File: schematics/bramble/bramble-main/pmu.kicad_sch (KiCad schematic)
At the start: 18 parts, among them J1 Conn_01x05_Pin, J6 Conn_01x03_Pin, SW1 STM_RESET, U3 STM32L031F6P6TR, U5 MCP1700x-120xxMB, Y1 Crystal

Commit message: pre-fab check-in of v2
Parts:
- renumbered C3 to C1, C4 to C2, C5 to C3, C24 to C4, C23 to C5, C21 to C7, C22 to C8, J6 to J2, R22 to R13, R23 to R14, R11 to R15, U5 to U4
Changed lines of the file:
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@@
 		(on_board yes)
 		(dnp no)
-		(property "Reference" "C23"
+		(property "Reference" "C5"
 			(at 161.29 123.1901 0)
 			(effects
@@
 			(project "bramble"
 				(path "/e35d7dcf-51bd-456f-89cf-e52d660079b4/df1d8afa-9717-44ff-901e-40cae4aada91"
-					(reference "C23")
+					(reference "C5")
 					(unit 1)
 				)
@@
 		(on_board yes)
 		(dnp no)
-		(property "Reference" "#U$07"
+		(property "Reference" "#U$012"
 			(at 92.71 90.17 0)
 			(effects
@@
 			(project "bramble"
 				(path "/e35d7dcf-51bd-456f-89cf-e52d660079b4/df1d8afa-9717-44ff-901e-40cae4aada91"
-					(reference "#U$07")
+					(reference "#U$012")
 					(unit 1)
 				)
@@
 		(on_board yes)
 		(dnp no)
-		(property "Reference" "#U$039"
+		(property "Reference" "#U$017"
 			(at 222.25 68.58 0)
 			(effects
@@
 			(project "bramble"
 				(path "/e35d7dcf-51bd-456f-89cf-e52d660079b4/df1d8afa-9717-44ff-901e-40cae4aada91"
-					(reference "#U$039")
+					(reference "#U$017")
 					(unit 1)
 				)
@@
 		(dnp no)
 		(fields_autoplaced yes)
-		(property "Reference" "C4"
+		(property "Reference" "C2"
 			(at 62.23 161.2899 0)
 			(effects
@@
 			(project "bramble"
 				(path "/e35d7dcf-51bd-456f-89cf-e52d660079b4/df1d8afa-9717-44ff-901e-40cae4aada91"
-					(reference "C4")
+					(reference "C2")
 					(unit 1)
 				)
@@
 		(dnp no)
 		(fields_autoplaced yes)
-		(property "Reference" "#PWR018"
+		(property "Reference" "#PWR011"
 			(at 125.095 158.115 0)
 			(effects
@@
 			(project ""
 				(path "/e35d7dcf-51bd-456f-89cf-e52d660079b4/df1d8afa-9717-44ff-901e-40cae4aada91"
-					(reference "#PWR018")
+					(reference "#PWR011")
 					(unit 1)
 				)
@@
 		(dnp no)
 		(fields_autoplaced yes)
-		(property "Reference" "#PWR05"
+		(property "Reference" "#PWR010"
 			(at 123.19 172.72 0)
 			(effects
@@
 			(project ""
 				(path "/e35d7dcf-51bd-456f-89cf-e52d660079b4/df1d8afa-9717-44ff-901e-40cae4aada91"
-					(reference "#PWR05")
+					(reference "#PWR010")
 					(unit 1)
 				)
@@
 		(dnp no)
 		(fields_autoplaced yes)
-		(property "Reference" "C5"
+		(property "Reference" "C3"
 			(at 76.2 161.2899 0)
 			(effects
@@
 			(project "bramble"
 				(path "/e35d7dcf-51bd-456f-89cf-e52d660079b4/df1d8afa-9717-44ff-901e-40cae4aada91"
-					(reference "C5")
+					(reference "C3")
 					(unit 1)
 				)
@@
 		(on_board yes)
 		(dnp no)
-		(property "Reference" "C22"
+		(property "Reference" "C8"
 			(at 226.06 62.2299 0)
 			(effects
@@
 			(project "bramble"
 				(path "/e35d7dcf-51bd-456f-89cf-e52d660079b4/df1d8afa-9717-44ff-901e-40cae4aada91"
-					(reference "C22")
+					(reference "C8")
 					(unit 1)
 				)
@@
 		(dnp no)
 		(fields_autoplaced yes)
-		(property "Reference" "#PWR016"
+		(property "Reference" "#PWR09"
 			(at 58.42 154.94 0)
 			(effects
@@
 			(project "bramble"
 				(path "/e35d7dcf-51bd-456f-89cf-e52d660079b4/df1d8afa-9717-44ff-901e-40cae4aada91"
-					(reference "#PWR016")
+					(reference "#PWR09")
 					(unit 1)
 				)
@@
 		(on_board yes)
 		(dnp no)
-		(property "Reference" "R22"
+		(property "Reference" "R13"
 			(at 79.502 84.328 90)
 			(effects
@@
 			(project "bramble"
 				(path "/e35d7dcf-51bd-456f-89cf-e52d660079b4/df1d8afa-9717-44ff-901e-40cae4aada91"
-					(reference "R22")
+					(reference "R13")
 					(unit 1)
 				)
@@
 		(on_board yes)
 		(dnp no)
-		(property "Reference" "C21"
+		(property "Reference" "C7"
 			(at 213.995 50.1649 0)
 			(effects
@@
 			(project "bramble"
 				(path "/e35d7dcf-51bd-456f-89cf-e52d660079b4/df1d8afa-9717-44ff-901e-40cae4aada91"
-					(reference "C21")
+					(reference "C7")
 					(unit 1)
 				)
@@
 		(on_board yes)
 		(dnp no)
-		(property "Reference" "C24"
+		(property "Reference" "C4"
 			(at 132.08 123.1901 0)
 			(effects
@@
 			(project "bramble"
 				(path "/e35d7dcf-51bd-456f-89cf-e52d660079b4/df1d8afa-9717-44ff-901e-40cae4aada91"
-					(reference "C24")
+					(reference "C4")
 					(unit 1)
 				)
@@
 		(dnp no)
 		(fields_autoplaced yes)
-		(property "Reference" "U5"
+		(property "Reference" "U4"
 			(at 148.59 111.76 0)
 			(effects
@@
 			(project ""
 				(path "/e35d7dcf-51bd-456f-89cf-e52d660079b4/df1d8afa-9717-44ff-901e-40cae4aada91"
-					(reference "U5")
+					(reference "U4")
 					(unit 1)
 				)
@@
 		(dnp no)
 		(fields_autoplaced yes)
-		(property "Reference" "R11"
+		(property "Reference" "R15"
 			(at 165.1 44.45 90)
 			(effects
@@
 			(project ""
 				(path "/e35d7dcf-51bd-456f-89cf-e52d660079b4/df1d8afa-9717-44ff-901e-40cae4aada91"
-					(reference "R11")
+					(reference "R15")
 					(unit 1)
 				)
@@
 		(on_board yes)
 		(dnp no)
-		(property "Reference" "#U$034"
+		(property "Reference" "#U$016"
 			(at 210.185 67.31 0)
 			(effects
@@
 			(project "bramble"
 				(path "/e35d7dcf-51bd-456f-89cf-e52d660079b4/df1d8afa-9717-44ff-901e-40cae4aada91"
-					(reference "#U$034")
+					(reference "#U$016")
 					(unit 1)
 				)
@@
 		(dnp no)
 		(fields_autoplaced yes)
-		(property "Reference" "#PWR014"
+		(property "Reference" "#PWR08"
 			(at 52.07 40.64 0)
 			(effects
@@
 			(project "bramble"
 				(path "/e35d7dcf-51bd-456f-89cf-e52d660079b4/df1d8afa-9717-44ff-901e-40cae4aada91"
-					(reference "#PWR014")
+					(reference "#PWR08")
 					(unit 1)
 				)
@@
 		(on_board yes)
 		(dnp no)
-		(property "Reference" "#U$09"
+		(property "Reference" "#U$014"
 			(at 196.85 85.09 0)
 			(effects
@@
 			(project "bramble"
 				(path "/e35d7dcf-51bd-456f-89cf-e52d660079b4/df1d8afa-9717-44ff-901e-40cae4aada91"
-					(reference "#U$09")
+					(reference "#U$014")
 					(unit 1)
 				)
@@
 		(on_board yes)
 		(dnp no)
-		(property "Reference" "#U$04"
+		(property "Reference" "#U$09"
 			(at 52.07 80.01 0)
 			(effects
@@
 			(project "bramble"
 				(path "/e35d7dcf-51bd-456f-89cf-e52d660079b4/df1d8afa-9717-44ff-901e-40cae4aada91"
-					(reference "#U$04")
+					(reference "#U$09")
 					(unit 1)
 				)
@@
 		(on_board yes)
 		(dnp no)
-		(property "Reference" "#U$010"
+		(property "Reference" "#U$013"
 			(at 148.59 135.89 0)
 			(effects
@@
 			(project "bramble"
 				(path "/e35d7dcf-51bd-456f-89cf-e52d660079b4/df1d8afa-9717-44ff-901e-40cae4aada91"
-					(reference "#U$010")
+					(reference "#U$013")
 					(unit 1)
 				)
@@
 		(on_board yes)
 		(dnp no)
-		(property "Reference" "#U$05"
+		(property "Reference" "#U$010"
 			(at 58.42 179.07 0)
 			(effects
@@
 			(project "bramble"
 				(path "/e35d7dcf-51bd-456f-89cf-e52d660079b4/df1d8afa-9717-44ff-901e-40cae4aada91"
-					(reference "#U$05")
+					(reference "#U$010")
 					(unit 1)
 				)
@@
 		(on_board yes)
 		(dnp no)
-		(property "Reference" "R23"
+		(property "Reference" "R14"
 			(at 84.582 84.328 90)
 			(effects
@@
 			(project "bramble"
 				(path "/e35d7dcf-51bd-456f-89cf-e52d660079b4/df1d8afa-9717-44ff-901e-40cae4aada91"
-					(reference "R23")
+					(reference "R14")
 					(unit 1)
 				)
@@
 		(dnp no)
 		(fields_autoplaced yes)
-		(property "Reference" "#PWR017"
+		(property "Reference" "#PWR012"
 			(at 165.1 116.84 0)
 			(effects
@@
 			(project "bramble"
 				(path "/e35d7dcf-51bd-456f-89cf-e52d660079b4/df1d8afa-9717-44ff-901e-40cae4aada91"
-					(reference "#PWR017")
+					(reference "#PWR012")
 					(unit 1)
 				)
@@
 		(on_board yes)
 		(dnp no)
-		(property "Reference" "#U$08"
+		(property "Reference" "#U$015"
 			(at 203.2 64.77 0)
 			(effects
@@
 			(project "bramble"
 				(path "/e35d7dcf-51bd-456f-89cf-e52d660079b4/df1d8afa-9717-44ff-901e-40cae4aada91"
-					(reference "#U$08")
+					(reference "#U$015")
 					(unit 1)
 				)
@@
 		(dnp no)
 		(fields_autoplaced yes)
-		(property "Reference" "#PWR015"
+		(property "Reference" "#PWR013"
 			(at 165.735 71.12 0)
 			(effects
@@
 			(project "bramble"
 				(path "/e35d7dcf-51bd-456f-89cf-e52d660079b4/df1d8afa-9717-44ff-901e-40cae4aada91"
-					(reference "#PWR015")
+					(reference "#PWR013")
 					(unit 1)
 				)
@@
 		(dnp no)
 		(fields_autoplaced yes)
-		(property "Reference" "C3"
+		(property "Reference" "C1"
 			(at 49.53 161.2899 0)
 			(effects
@@
 			(project ""
 				(path "/e35d7dcf-51bd-456f-89cf-e52d660079b4/df1d8afa-9717-44ff-901e-40cae4aada91"
-					(reference "C3")
+					(reference "C1")
 					(unit 1)
 				)
@@
 		(on_board yes)
 		(dnp no)
-		(property "Reference" "#U$06"
+		(property "Reference" "#U$011"
 			(at 80.01 110.49 0)
 			(effects
@@
 			(project "bramble"
 				(path "/e35d7dcf-51bd-456f-89cf-e52d660079b4/df1d8afa-9717-44ff-901e-40cae4aada91"
-					(reference "#U$06")
+					(reference "#U$011")
 					(unit 1)
 				)
@@
 		(dnp no)
 		(fields_autoplaced yes)
-		(property "Reference" "J6"
+		(property "Reference" "J2"
 			(at 111.125 153.67 0)
 			(effects
@@
 			(project ""
 				(path "/e35d7dcf-51bd-456f-89cf-e52d660079b4/df1d8afa-9717-44ff-901e-40cae4aada91"
-					(reference "J6")
-					(unit 1)
-				)
+					(reference "J2")
+					(unit 1)
+				)

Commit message: Checking before rollback
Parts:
- renumbered J2 to PWR1, J1 to STM_DEBUG1, D1 to STM_STATUS1, U3 to U2, U4 to U3
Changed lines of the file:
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@@
 		(dnp no)
 		(fields_autoplaced yes)
-		(property "Reference" "J1"
+		(property "Reference" "STM_DEBUG1"
 			(at 34.925 40.64 0)
 			(effects
@@
 			(project ""
 				(path "/e35d7dcf-51bd-456f-89cf-e52d660079b4/df1d8afa-9717-44ff-901e-40cae4aada91"
-					(reference "J1")
+					(reference "STM_DEBUG1")
 					(unit 1)
 				)
@@
 		(dnp no)
 		(fields_autoplaced yes)
-		(property "Reference" "D1"
+		(property "Reference" "STM_STATUS1"
 			(at 86.36 93.9164 90)
 			(effects
@@
 			(project ""
 				(path "/e35d7dcf-51bd-456f-89cf-e52d660079b4/df1d8afa-9717-44ff-901e-40cae4aada91"
-					(reference "D1")
+					(reference "STM_STATUS1")
 					(unit 1)
 				)
@@
 		(dnp no)
 		(fields_autoplaced yes)
-		(property "Reference" "U4"
+		(property "Reference" "U3"
 			(at 148.59 111.76 0)
 			(effects
@@
 			(project ""
 				(path "/e35d7dcf-51bd-456f-89cf-e52d660079b4/df1d8afa-9717-44ff-901e-40cae4aada91"
-					(reference "U4")
+					(reference "U3")
 					(unit 1)
 				)
@@
 		(dnp no)
 		(fields_autoplaced yes)
-		(property "Reference" "U3"
+		(property "Reference" "U2"
 			(at 124.46 38.1 0)
 			(effects
@@
 			(project "bramble"
 				(path "/e35d7dcf-51bd-456f-89cf-e52d660079b4/df1d8afa-9717-44ff-901e-40cae4aada91"
-					(reference "U3")
+					(reference "U2")
 					(unit 1)
 				)
@@
 		(dnp no)
 		(fields_autoplaced yes)
-		(property "Reference" "J2"
+		(property "Reference" "PWR1"
 			(at 111.125 153.67 0)
 			(effects
@@
 			(project ""
 				(path "/e35d7dcf-51bd-456f-89cf-e52d660079b4/df1d8afa-9717-44ff-901e-40cae4aada91"
-					(reference "J2")
-					(unit 1)
-				)
+					(reference "PWR1")
+					(unit 1)
+				)

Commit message: Check in some of the v3 change
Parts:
- renumbered STM_STATUS1 to D1, STM_DEBUG1 to J1, PWR1 to J2
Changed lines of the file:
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@@
 		(dnp no)
 		(fields_autoplaced yes)
-		(property "Reference" "STM_DEBUG1"
+		(property "Reference" "J1"
 			(at 34.925 40.64 0)
 			(effects
@@
 			(project ""
 				(path "/e35d7dcf-51bd-456f-89cf-e52d660079b4/df1d8afa-9717-44ff-901e-40cae4aada91"
-					(reference "STM_DEBUG1")
+					(reference "J1")
 					(unit 1)
 				)
@@
 		(dnp no)
 		(fields_autoplaced yes)
-		(property "Reference" "STM_STATUS1"
+		(property "Reference" "D1"
 			(at 86.36 93.9164 90)
 			(effects
@@
 			(project ""
 				(path "/e35d7dcf-51bd-456f-89cf-e52d660079b4/df1d8afa-9717-44ff-901e-40cae4aada91"
-					(reference "STM_STATUS1")
+					(reference "D1")
 					(unit 1)
 				)
@@
 		(dnp no)
 		(fields_autoplaced yes)
-		(property "Reference" "PWR1"
+		(property "Reference" "J2"
 			(at 111.125 153.67 0)
 			(effects
@@
 			(project ""
 				(path "/e35d7dcf-51bd-456f-89cf-e52d660079b4/df1d8afa-9717-44ff-901e-40cae4aada91"
-					(reference "PWR1")
-					(unit 1)
-				)
+					(reference "J2")
+					(unit 1)
+				)

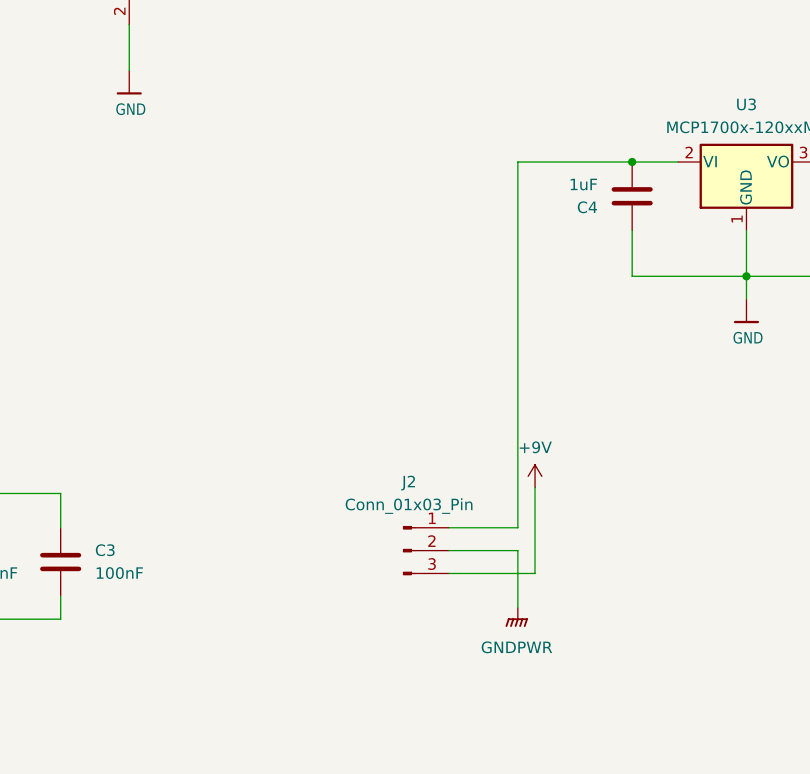
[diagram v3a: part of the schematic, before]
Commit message: Switch to 2x 2 pin JST connectors and wire them in series on board
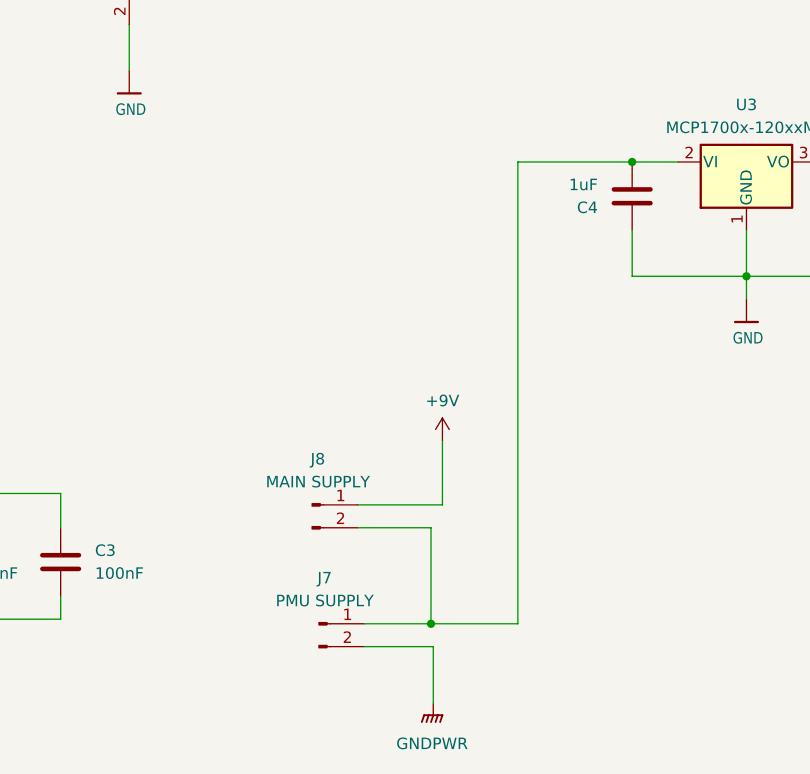
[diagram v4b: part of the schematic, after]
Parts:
- removed J2: Conn_01x03_Pin, Connector_JST:JST_XH_B3B-XH-AM_1x03_P2.50mm_Vertical, symbol Connector:Conn_01x03_Pin
- added J7: PMU SUPPLY, Connector_JST:JST_PH_B2B-PH-K_1x02_P2.00mm_Vertical, symbol Connector:Conn_01x02_Pin
- added J8: MAIN SUPPLY, Connector_JST:JST_PH_B2B-PH-K_1x02_P2.00mm_Vertical, symbol Connector:Conn_01x02_Pin
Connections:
- net +9V: now also J8.1 (Pin_1)
- net GNDPWR: now also J7.2 (Pin_2)
- net at C4.2, U3.2 (VI): now also J7.1 (Pin_1), J8.2 (Pin_2)
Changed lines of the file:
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@@
 		(color 0 0 0 0)
 	)
-	(wire
-		(pts
-			(xy 115.57 163.83) (xy 125.095 163.83)
-		)
-		(stroke
-			(width 0)
-			(type default)
-		)
+	(junction
+		(at 113.538 169.418)
+		(diameter 0)
+		(color 0 0 0 0)
 	)
 	(wire
@@
 	(wire
 		(pts
+			(xy 113.538 169.418) (xy 123.19 169.418)
+		)
+		(stroke
+			(width 0)
+			(type default)
+		)
+	)
+	(wire
+		(pts
 			(xy 191.77 76.2) (xy 196.85 76.2)
 		)
@@
 	(wire
 		(pts
+			(xy 106.172 169.418) (xy 113.538 169.418)
+		)
+		(stroke
+			(width 0)
+			(type default)
+		)
+	)
+	(wire
+		(pts
 			(xy 196.85 76.2) (xy 196.85 82.55)
 		)
@@
 	(wire
 		(pts
+			(xy 105.41 158.75) (xy 113.538 158.75)
+		)
+		(stroke
+			(width 0)
+			(type default)
+		)
+	)
+	(wire
+		(pts
 			(xy 222.25 47.625) (xy 222.25 58.42)
 		)
@@
 	(wire
 		(pts
-			(xy 125.095 154.305) (xy 125.095 163.83)
+			(xy 105.41 156.21) (xy 114.808 156.21)
 		)
 		(stroke
@@
 	(wire
 		(pts
-			(xy 115.57 158.75) (xy 123.19 158.75)
-		)
-		(stroke
-			(width 0)
-			(type default)
-		)
-	)
-	(wire
-		(pts
 			(xy 196.85 63.5) (xy 196.85 76.2)
 		)
@@
 	(wire
 		(pts
+			(xy 113.538 158.75) (xy 113.538 169.418)
+		)
+		(stroke
+			(width 0)
+			(type default)
+		)
+	)
+	(wire
+		(pts
 			(xy 58.42 151.13) (xy 58.42 154.94)
 		)
@@
 	(wire
 		(pts
+			(xy 114.808 149.098) (xy 114.808 156.21)
+		)
+		(stroke
+			(width 0)
+			(type default)
+		)
+	)
+	(wire
+		(pts
 			(xy 52.07 36.83) (xy 52.07 45.72)
 		)
@@
 	(wire
 		(pts
-			(xy 115.57 161.29) (xy 123.19 161.29)
+			(xy 106.172 171.958) (xy 113.792 171.958)
 		)
 		(stroke
@@
 	(wire
 		(pts
-			(xy 123.19 161.29) (xy 123.19 167.64)
-		)
-		(stroke
-			(width 0)
-			(type default)
-		)
-	)
-	(wire
-		(pts
-			(xy 123.19 118.11) (xy 123.19 158.75)
+			(xy 113.792 171.958) (xy 113.792 178.308)
+		)
+		(stroke
+			(width 0)
+			(type default)
+		)
+	)
+	(wire
+		(pts
+			(xy 123.19 118.11) (xy 123.19 169.418)
 		)
 		(stroke
@@
 	(symbol
 		(lib_id "power:+9V")
-		(at 125.095 154.305 0)
+		(at 114.808 149.098 0)
 		(unit 1)
 		(exclude_from_sim no)
@@
 		(fields_autoplaced yes)
 		(property "Reference" "#PWR011"
-			(at 125.095 158.115 0)
+			(at 114.808 152.908 0)
 			(effects
 				(font
@@
 		)
 		(property "Value" "+9V"
-			(at 125.095 149.86 0)
+			(at 114.808 144.653 0)
 			(effects
 				(font
@@
 		)
 		(property "Footprint" ""
-			(at 125.095 154.305 0)
+			(at 114.808 149.098 0)
 			(effects
 				(font
@@
 		)
 		(property "Datasheet" ""
-			(at 125.095 154.305 0)
+			(at 114.808 149.098 0)
 			(effects
 				(font
@@
 		)
 		(property "Description" "Power symbol creates a global label with name \"+9V\""
-			(at 125.095 154.305 0)
+			(at 114.808 149.098 0)
 			(effects
 				(font
@@
 	(symbol
 		(lib_id "power:GNDPWR")
-		(at 123.19 167.64 0)
+		(at 113.792 178.308 0)
 		(unit 1)
 		(exclude_from_sim no)
@@
 		(fields_autoplaced yes)
 		(property "Reference" "#PWR010"
-			(at 123.19 172.72 0)
+			(at 113.792 183.388 0)
 			(effects
 				(font
@@
 		)
 		(property "Value" "GNDPWR"
-			(at 123.063 172.085 0)
+			(at 113.665 182.753 0)
 			(effects
 				(font
@@
 		)
 		(property "Footprint" ""
-			(at 123.19 168.91 0)
+			(at 113.792 179.578 0)
 			(effects
 				(font
@@
 		)
 		(property "Datasheet" ""
-			(at 123.19 168.91 0)
+			(at 113.792 179.578 0)
 			(effects
 				(font
@@
 		)
 		(property "Description" "Power symbol creates a global label with name \"GNDPWR\" , global ground"
-			(at 123.19 167.64 0)
+			(at 113.792 178.308 0)
 			(effects
 				(font
@@
 				(path "/e35d7dcf-51bd-456f-89cf-e52d660079b4/df1d8afa-9717-44ff-901e-40cae4aada91"
 					(reference "#PWR010")
+					(unit 1)
+				)
+			)
+		)
+	)
+	(symbol
+		(lib_id "Connector:Conn_01x02_Pin")
+		(at 101.092 169.418 0)
+		(unit 1)
+		(exclude_from_sim no)
+		(in_bom yes)
+		(on_board yes)
+		(dnp no)
+		(fields_autoplaced yes)
+		(property "Reference" "J7"
+			(at 101.727 164.338 0)
+			(effects
+				(font
+					(size 1.27 1.27)
+				)
+			)
+		)
+		(property "Value" "PMU SUPPLY"
+			(at 101.727 166.878 0)
+			(effects
+				(font
+					(size 1.27 1.27)
+				)
+			)
+		)
+		(property "Footprint" "Connector_JST:JST_PH_B2B-PH-K_1x02_P2.00mm_Vertical"
+			(at 101.092 169.418 0)
+			(effects
+				(font
+					(size 1.27 1.27)
+				)
+				(hide yes)
+			)
+		)
+		(property "Datasheet" "~"
+			(at 101.092 169.418 0)
+			(effects
+				(font
+					(size 1.27 1.27)
+				)
+				(hide yes)
+			)
+		)
+		(property "Description" "Generic connector, single row, 01x02, script generated"
+			(at 101.092 169.418 0)
+			(effects
+				(font
+					(size 1.27 1.27)
+				)
+				(hide yes)
+			)
+		)
+		(pin "2"
+		)
+		(pin "1"
+		)
+		(instances
+			(project ""
+				(path "/e35d7dcf-51bd-456f-89cf-e52d660079b4/df1d8afa-9717-44ff-901e-40cae4aada91"
+					(reference "J7")
 					(unit 1)
 				)
@@
 	)
 	(symbol
+		(lib_id "Connector:Conn_01x02_Pin")
+		(at 100.33 156.21 0)
+		(unit 1)
+		(exclude_from_sim no)
+		(in_bom yes)
+		(on_board yes)
+		(dnp no)
+		(fields_autoplaced yes)
+		(property "Reference" "J8"
+			(at 100.965 151.13 0)
+			(effects
+				(font
+					(size 1.27 1.27)
+				)
+			)
+		)
+		(property "Value" "MAIN SUPPLY"
+			(at 100.965 153.67 0)
+			(effects
+				(font
+					(size 1.27 1.27)
+				)
+			)
+		)
+		(property "Footprint" "Connector_JST:JST_PH_B2B-PH-K_1x02_P2.00mm_Vertical"
+			(at 100.33 156.21 0)
+			(effects
+				(font
+					(size 1.27 1.27)
+				)
+				(hide yes)
+			)
+		)
+		(property "Datasheet" "~"
+			(at 100.33 156.21 0)
+			(effects
+				(font
+					(size 1.27 1.27)
+				)
+				(hide yes)
+			)
+		)
+		(property "Description" "Generic connector, single row, 01x02, script generated"
+			(at 100.33 156.21 0)
+			(effects
+				(font
+					(size 1.27 1.27)
+				)
+				(hide yes)
+			)
+		)
+		(pin "2"
+		)
+		(pin "1"
+		)
+		(instances
+			(project "bramble"
+				(path "/e35d7dcf-51bd-456f-89cf-e52d660079b4/df1d8afa-9717-44ff-901e-40cae4aada91"
+					(reference "J8")
+					(unit 1)
+				)
+			)
+		)
+	)
+	(symbol
 		(lib_id "Adafruit Feather RP2040 RFM-eagle-import:GND")
 		(at 210.185 67.31 0)
@@
 					(unit 1)
 				)
-			)
-		)
-	)
-	(symbol
-		(lib_id "Connector:Conn_01x03_Pin")
-		(at 110.49 161.29 0)
-		(unit 1)
-		(exclude_from_sim no)
-		(in_bom yes)
-		(on_board yes)
-		(dnp no)
-		(fields_autoplaced yes)
-		(property "Reference" "J2"
-			(at 111.125 153.67 0)
-			(effects
-				(font
-					(size 1.27 1.27)
-				)
-			)
-		)
-		(property "Value" "Conn_01x03_Pin"
-			(at 111.125 156.21 0)
-			(effects
-				(font
-					(size 1.27 1.27)
-				)
-			)
-		)
-		(property "Footprint" "Connector_JST:JST_XH_B3B-XH-AM_1x03_P2.50mm_Vertical"
-			(at 110.49 161.29 0)
-			(effects
-				(font
-					(size 1.27 1.27)
-				)
-				(hide yes)
-			)
-		)
-		(property "Datasheet" "~"
-			(at 110.49 161.29 0)
-			(effects
-				(font
-					(size 1.27 1.27)
-				)
-				(hide yes)
-			)
-		)
-		(property "Description" "Generic connector, single row, 01x03, script generated"
-			(at 110.49 161.29 0)
-			(effects
-				(font
-					(size 1.27 1.27)
-				)
-				(hide yes)
-			)
-		)
-		(pin "1"
-		)
-		(pin "2"
-		)
-		(pin "3"
-		)
-		(instances
-			(project ""
-				(path "/e35d7dcf-51bd-456f-89cf-e52d660079b4/df1d8afa-9717-44ff-901e-40cae4aada91"
-					(reference "J2")
-					(unit 1)
-				)
